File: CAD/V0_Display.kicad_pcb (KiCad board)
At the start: 4 copper layers, 80 x 35 mm, 46 parts, among them J2 I2C Header 1, J3 SWD, J4 USB-TYPE-C-018, J7 USB_Header, J8 Conn_01x02, SW1 RESET, SW5 BOOTSEL, SW6 Killswitch, SW7 Rotary_Encoder_Switch, U1 AP2127K-3.3, U2 USBLC6-2P6, U3 74LVC1G17, U4 W25Q16JVUXIQ_TR, U5 RP2040, Y1 12Mhz

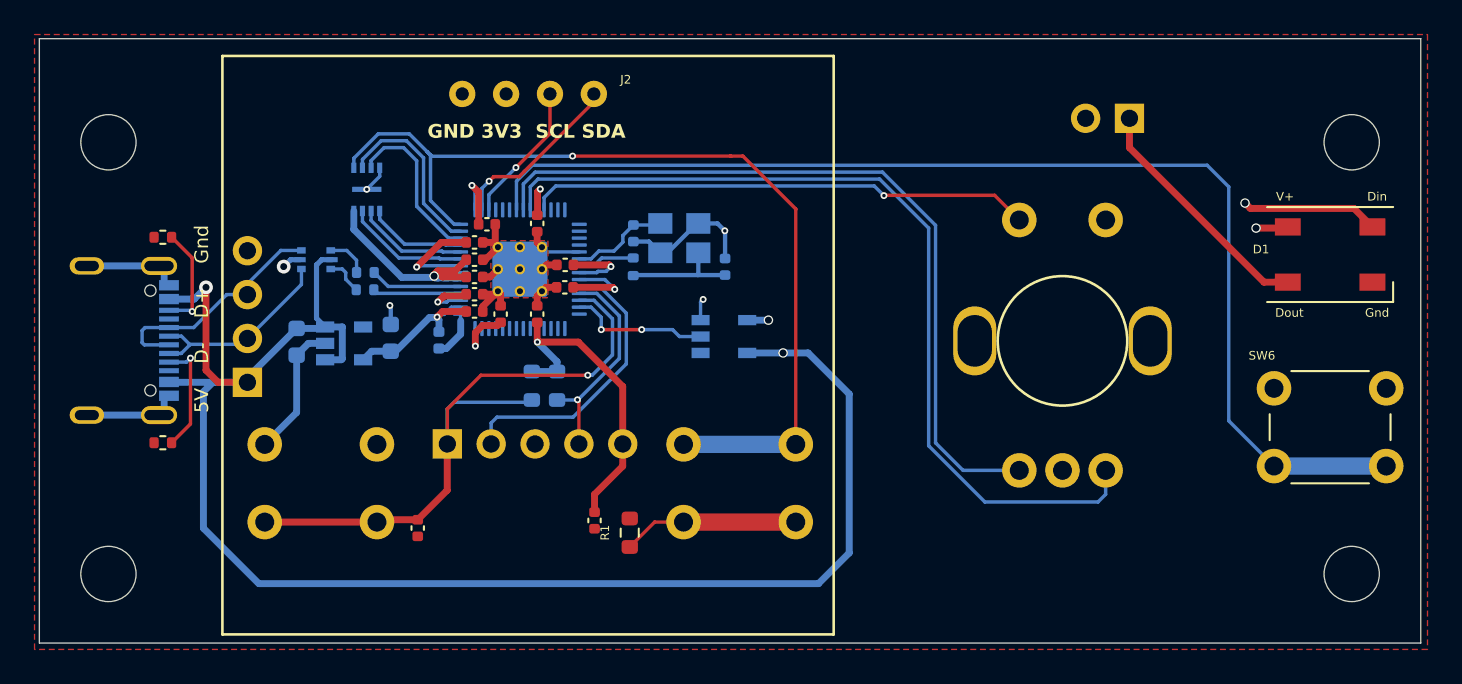
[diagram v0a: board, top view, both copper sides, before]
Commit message: Reworked board to 2-layer
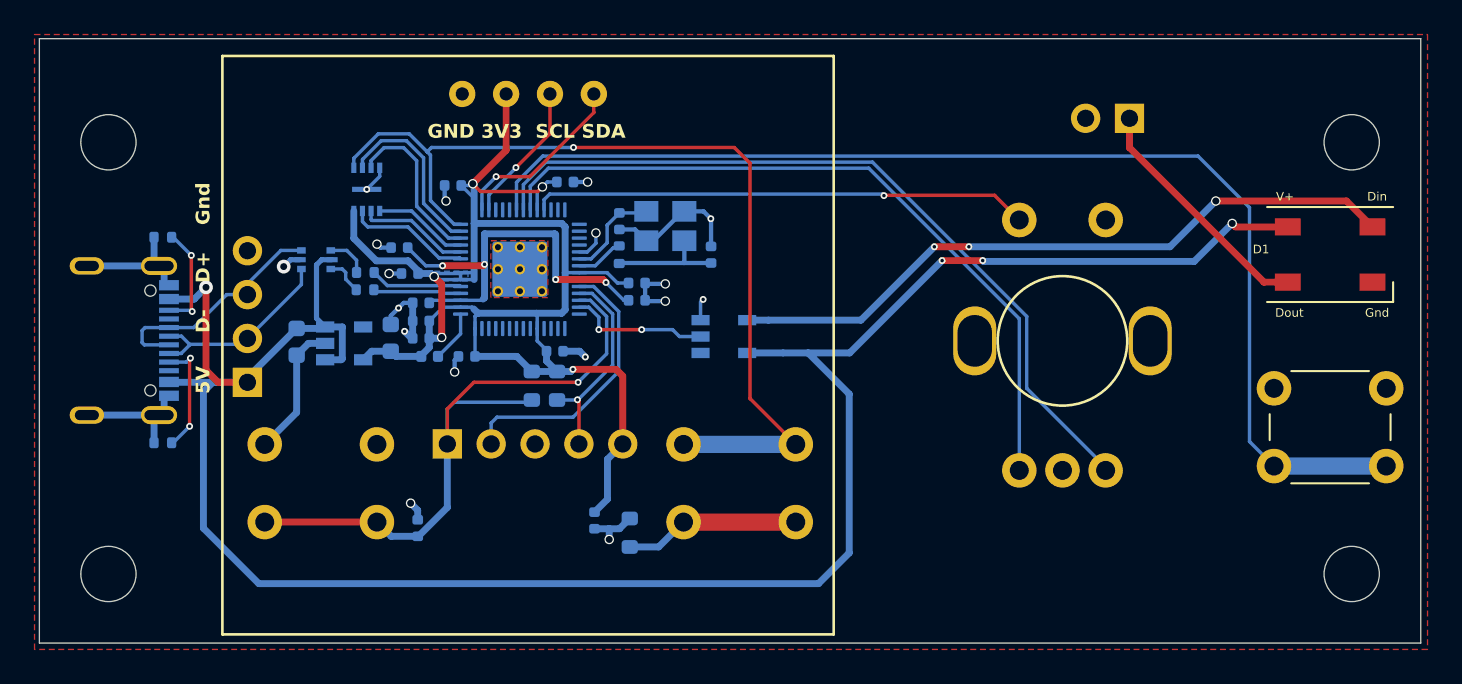
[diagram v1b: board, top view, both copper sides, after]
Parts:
- C10: value 0.1uf -> 1uf; moved to B.Cu
- C11, C12, C13, C14, C15, C16, C17, C5, C6, C7, C8, C9, R1, R5, R6: moved to B.Cu
- C3, C4: value 27pf -> 30pf
- moved C10 6.87 mm to (107.3, 67.0), turned to 180 degrees
- moved C17 5.30 mm to (106.6, 63.2), turned to 180 degrees
- moved C7 5.12 mm to (106.0, 61.8), turned to 180 degrees
- moved C9 4.68 mm to (107.3, 65.0), turned to 180 degrees
- moved C14 4.62 mm to (109.9, 68.0), turned to 180 degrees
- moved C12 4.48 mm to (109.1, 58.1), turned to 180 degrees
- moved C11 4.28 mm to (119.8, 63.8), turned to 0 degrees
- moved C6 4.24 mm to (119.8, 64.8), turned to 0 degrees
- moved C15 3.81 mm to (115.0, 67.8), turned to 0 degrees
- moved C16 3.15 mm to (107.3, 66.0), turned to 180 degrees
- moved C13 2.90 mm to (115.6, 58.0), turned to 0 degrees
- moved L1 1.08 mm to (107.8, 68.0), turned to 0 degrees
- moved C4 1.07 mm to (124.1, 62.2)
- moved R2 1.07 mm to (118.8, 62.2)
- moved Y1 1.07 mm to (121.4, 60.5)
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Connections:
- U5 pad 8: Encoder_A -> Encoder_B
- U5 pad 9: Encoder_B -> Encoder_A
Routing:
- net 3.3V: track 58.3 -> 90.2 mm, vias 7 -> 5
- net 1.1V: track 13.9 -> 26.1 mm, vias 3 -> 4
- net GND: track 48.5 -> 54.9 mm, vias 5 -> 17
- net Encoder_B: track 51.5 -> 45.7 mm
- net VBUS: track 128.6 -> 125.4 mm, vias 3 -> 4
- net Encoder_A: track 45.0 -> 42.5 mm
- net Net-(D1-DIN): track 40.8 -> 39.7 mm, vias 2 -> 3
- net RUN: track 38.5 -> 39.1 mm
- net SWDCLK: track 16.8 -> 16.2 mm
- net OSC_OUT: track 3.31 -> 2.79 mm
- net Net-(J4-CC2): track 6.45 -> 6.50 mm, vias 1 -> 2
- net Net-(J4-CC1): track 6.97 -> 7.02 mm, vias 1 -> 2
- removed copper zone on In1.Cu, net 1.1V
- removed copper zone on In2.Cu, net 3.3V
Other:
- copper layers 4 -> 2
